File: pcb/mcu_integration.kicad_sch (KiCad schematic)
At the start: 39 parts, among them IC2 LMT87DCKT, J5 DM3BT-DSF-PEJS, U1 STM32F103RBTx, U8 LTC4300A-1IMS8_PBF, Y1 ECS-80-18-5PX-GM-TR

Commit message: Started selecting BOM
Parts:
- C1, C2, C27, C3, C4, C44, C6, C9: Manufacturer_Name (none) -> Kemet; Manufacturer_Part_Number (none) -> C0402C104K8RACAUTO
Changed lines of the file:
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@@
+			)
+		)
+		(property "Manufacturer_Name" "Kemet"
+			(at 49.53 62.23 90)
+			(effects
+				(font
+					(size 1.27 1.27)
+				)
+				(hide yes)
+			)
+		)
+		(property "Manufacturer_Part_Number" "C0402C104K8RACAUTO"
+			(at 49.53 62.23 90)
+			(effects
+				(font
+					(size 1.27 1.27)
+				)
+				(hide yes)
 			)
 		)
@@
 			)
 		)
+		(property "Manufacturer_Name" "Kemet"
+			(at 118.11 24.13 0)
+			(effects
+				(font
+					(size 1.27 1.27)
+				)
+				(hide yes)
+			)
+		)
+		(property "Manufacturer_Part_Number" "C0402C104K8RACAUTO"
+			(at 118.11 24.13 0)
+			(effects
+				(font
+					(size 1.27 1.27)
+				)
+				(hide yes)
+			)
+		)
 		(pin "1"
 		)
@@
 			)
 		)
+		(property "Manufacturer_Name" "Kemet"
+			(at 27.94 27.94 0)
+			(effects
+				(font
+					(size 1.27 1.27)
+				)
+				(hide yes)
+			)
+		)
+		(property "Manufacturer_Part_Number" "C0402C104K8RACAUTO"
+			(at 27.94 27.94 0)
+			(effects
+				(font
+					(size 1.27 1.27)
+				)
+				(hide yes)
+			)
+		)
 		(pin "1"
 		)
@@
 			)
 		)
+		(property "Manufacturer_Name" "Kemet"
+			(at 76.2 27.94 0)
+			(effects
+				(font
+					(size 1.27 1.27)
+				)
+				(hide yes)
+			)
+		)
+		(property "Manufacturer_Part_Number" "C0402C104K8RACAUTO"
+			(at 76.2 27.94 0)
+			(effects
+				(font
+					(size 1.27 1.27)
+				)
+				(hide yes)
+			)
+		)
 		(pin "1"
 		)
@@
 		)
 		(property "Description" ""
+			(at 204.47 55.88 0)
+			(effects
+				(font
+					(size 1.27 1.27)
+				)
+				(hide yes)
+			)
+		)
+		(property "Manufacturer_Name" "Kemet"
+			(at 204.47 55.88 0)
+			(effects
+				(font
+					(size 1.27 1.27)
+				)
+				(hide yes)
+			)
+		)
+		(property "Manufacturer_Part_Number" "C0402C104K8RACAUTO"
 			(at 204.47 55.88 0)
 			(effects
@@
 			)
 		)
+		(property "Manufacturer_Name" "Kemet"
+			(at 63.5 27.94 0)
+			(effects
+				(font
+					(size 1.27 1.27)
+				)
+				(hide yes)
+			)
+		)
+		(property "Manufacturer_Part_Number" "C0402C104K8RACAUTO"
+			(at 63.5 27.94 0)
+			(effects
+				(font
+					(size 1.27 1.27)
+				)
+				(hide yes)
+			)
+		)
 		(pin "1"
 		)
@@
 			)
 		)
+		(property "Manufacturer_Name" "Kemet"
+			(at 39.37 27.94 0)
+			(effects
+				(font
+					(size 1.27 1.27)
+				)
+				(hide yes)
+			)
+		)
+		(property "Manufacturer_Part_Number" "C0402C104K8RACAUTO"
+			(at 39.37 27.94 0)
+			(effects
+				(font
+					(size 1.27 1.27)
+				)
+				(hide yes)
+			)
+		)
 		(pin "1"
 		)
@@
 			(at 52.07 27.94 0)
 			(effects
+				(font
+					(size 1.27 1.27)
+				)
+				(hide yes)
+			)
+		)
+		(property "Manufacturer_Name" "Kemet"
+			(at 52.07 27.94 0)
+			(effects
+				(font
+					(size 1.27 1.27)
+				)
+				(hide yes)
+			)
+		)
+		(property "Manufacturer_Part_Number" "C0402C104K8RACAUTO"
+			(at 52.07 27.94 0)
+			(effects

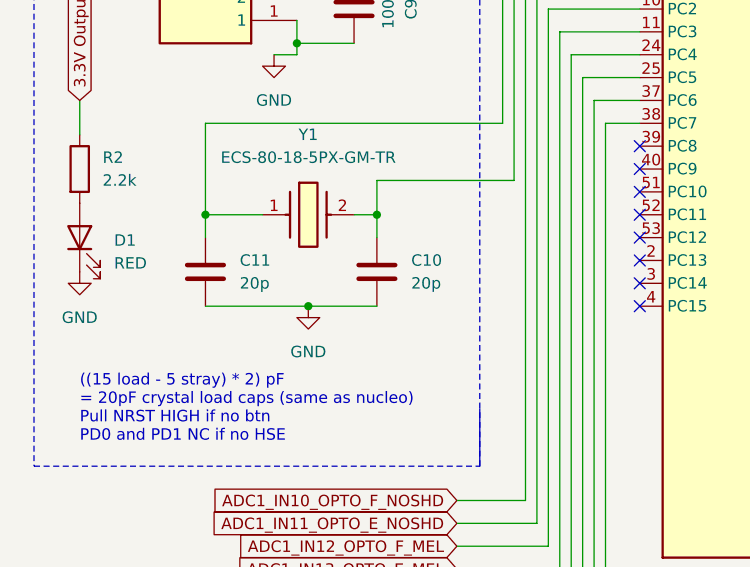
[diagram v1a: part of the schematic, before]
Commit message: Added more to the BOM
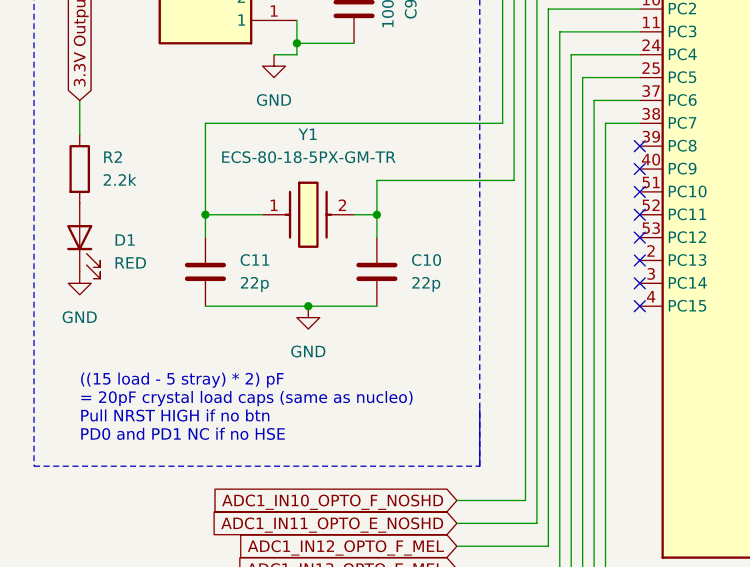
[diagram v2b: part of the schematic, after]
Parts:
- C1, C2, C27, C3, C4, C44, C6, C9: Manufacturer_Name Kemet -> Murata; Manufacturer_Part_Number C0402C104K8RACAUTO -> GCM155R71C104KA55D
- C10, C11: value 20p -> 22p; Manufacturer_Name (none) -> Murata; Manufacturer_Part_Number (none) -> GCM1555C1H220JA16D
- C33, C7, C8: Manufacturer_Name (none) -> Murata; Manufacturer_Part_Number (none) -> GRT155R61C105KE01D
- C45, C49: Manufacturer_Name (none) -> Murata; Manufacturer_Part_Number (none) -> GCM155R71H103KA55D
- C48: Manufacturer_Name (none) -> Murata; Manufacturer_Part_Number (none) -> GCM1555C1H221JA16D
- C5: Manufacturer_Name (none) -> Murata; Manufacturer_Part_Number (none) -> GRT188R61C106KE13D
- R1, R2: Manufacturer_Name (none) -> Panasonic; Manufacturer_Part_Number (none) -> ERJ-2RKF2200X
- R10, R13, R14, R9: Manufacturer_Name (none) -> Panasonic; Manufacturer_Part_Number (none) -> ERJ-H2RF1002X

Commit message: Finished BOM and fixed file paths for 3D models
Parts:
- D1, J_SWD+UART1, MH1, MH2, MH3, MH4, SH1, SH2, SH3: now not fitted
- FB1: Manufacturer_Name (none) -> Murata; Manufacturer_Part_Number (none) -> BLM18SG121TN1D
- J5: Manufacturer_Name (none) -> Hirose; Manufacturer_Part_Number (none) -> DM3BT-DSF-PEJS
- U1: Manufacturer_Name (none) -> STMicroelectronics; Manufacturer_Part_Number (none) -> STM32F103RBT7
- U8: Manufacturer_Name (none) -> Analog Devices; Manufacturer_Part_Number (none) -> LTC4300A-1IMS8#PBF
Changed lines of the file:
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@@
 		(in_bom yes)
 		(on_board yes)
-		(dnp no)
+		(dnp yes)
 		(property "Reference" "MH4"
 			(at 211.074 100.33 90)
@@
 			)
 		)
+		(property "Manufacturer_Name" "Hirose"
+			(at 219.71 33.02 0)
+			(effects
+				(font
+					(size 1.27 1.27)
+				)
+				(hide yes)
+			)
+		)
+		(property "Manufacturer_Part_Number" "DM3BT-DSF-PEJS"
+			(at 219.71 33.02 0)
+			(effects
+				(font
+					(size 1.27 1.27)
+				)
+				(hide yes)
+			)
+		)
 		(pin "5"
 		)
@@
 		(in_bom yes)
 		(on_board yes)
-		(dnp no)
+		(dnp yes)
 		(property "Reference" "SH3"
 			(at 273.05 81.534 0)
@@
 			)
 		)
+		(property "Manufacturer_Name" "STMicroelectronics"
+			(at 99.06 80.01 0)
+			(effects
+				(font
+					(size 1.27 1.27)
+				)
+				(hide yes)
+			)
+		)
+		(property "Manufacturer_Part_Number" "STM32F103RBT7"
+			(at 99.06 80.01 0)
+			(effects
+				(font
+					(size 1.27 1.27)
+				)
+				(hide yes)
+			)
+		)
 		(pin "1"
 		)
@@
 		(in_bom yes)
 		(on_board yes)
-		(dnp no)
+		(dnp yes)
 		(fields_autoplaced yes)
 		(property "Reference" "MH2"
@@
 		(in_bom yes)
 		(on_board yes)
-		(dnp no)
+		(dnp yes)
 		(fields_autoplaced yes)
 		(property "Reference" "MH3"
@@
 		(in_bom yes)
 		(on_board yes)
-		(dnp no)
+		(dnp yes)
 		(property "Reference" "SH2"
 			(at 260.35 81.534 0)
@@
 		(in_bom yes)
 		(on_board yes)
-		(dnp no)
+		(dnp yes)
 		(fields_autoplaced yes)
 		(property "Reference" "D1"
@@
 			)
 		)
+		(property "Manufacturer_Name" "Murata"
+			(at 144.78 20.32 90)
+			(effects
+				(font
+					(size 1.27 1.27)
+				)
+				(hide yes)
+			)
+		)
+		(property "Manufacturer_Part_Number" "BLM18SG121TN1D"
+			(at 144.78 20.32 90)
+			(effects
+				(font
+					(size 1.27 1.27)
+				)
+				(hide yes)
+			)
+		)
 		(pin "1"
 		)
@@
 		(in_bom yes)
 		(on_board yes)
-		(dnp no)
+		(dnp yes)
 		(property "Reference" "SH1"
 			(at 247.65 81.28 0)
@@
 		(in_bom yes)
 		(on_board yes)
-		(dnp no)
+		(dnp yes)
 		(property "Reference" "J_SWD+UART1"
 			(at 171.45 66.0399 0)
@@
 		(in_bom yes)
 		(on_board yes)
-		(dnp no)
+		(dnp yes)
 		(fields_autoplaced yes)
 		(property "Reference" "MH1"
@@
 				(hide yes)
 			)
+		)
+		(property "Manufacturer_Name" "Analog Devices"
+			(at 45.72 168.91 0)
+			(effects
+				(font
+					(size 1.27 1.27)
+				)
+				(hide yes)
+			)
+		)
+		(property "Manufacturer_Part_Number" "LTC4300A-1IMS8#PBF"
+			(at 45.72 168.91 0)
+			(effects
+				(font
+					(size 1.27 1.27)
+				)
+				(hide yes)
+			)

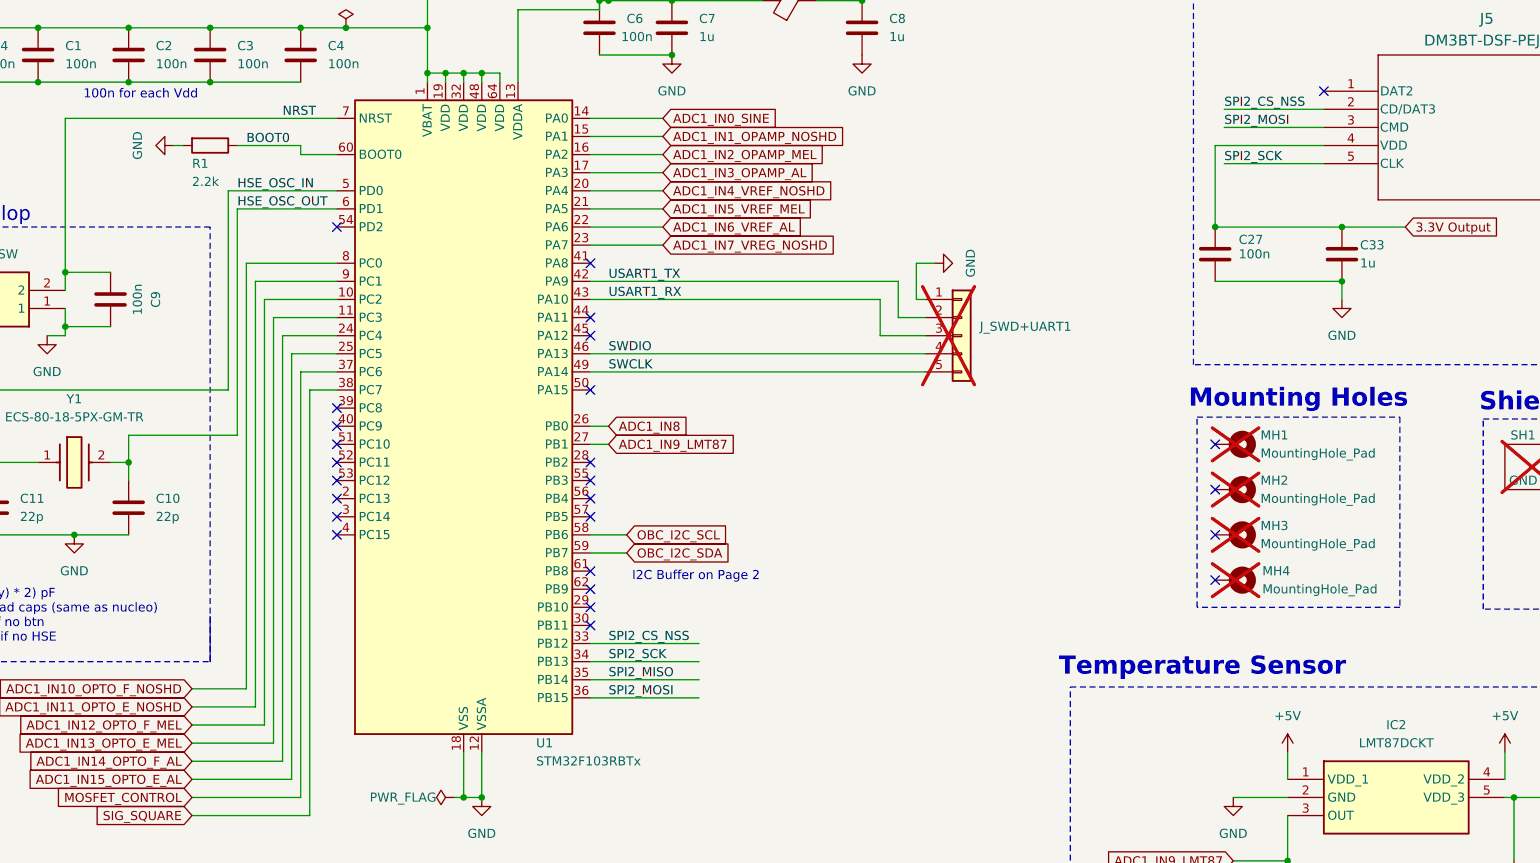
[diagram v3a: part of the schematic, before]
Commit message: updated component labels
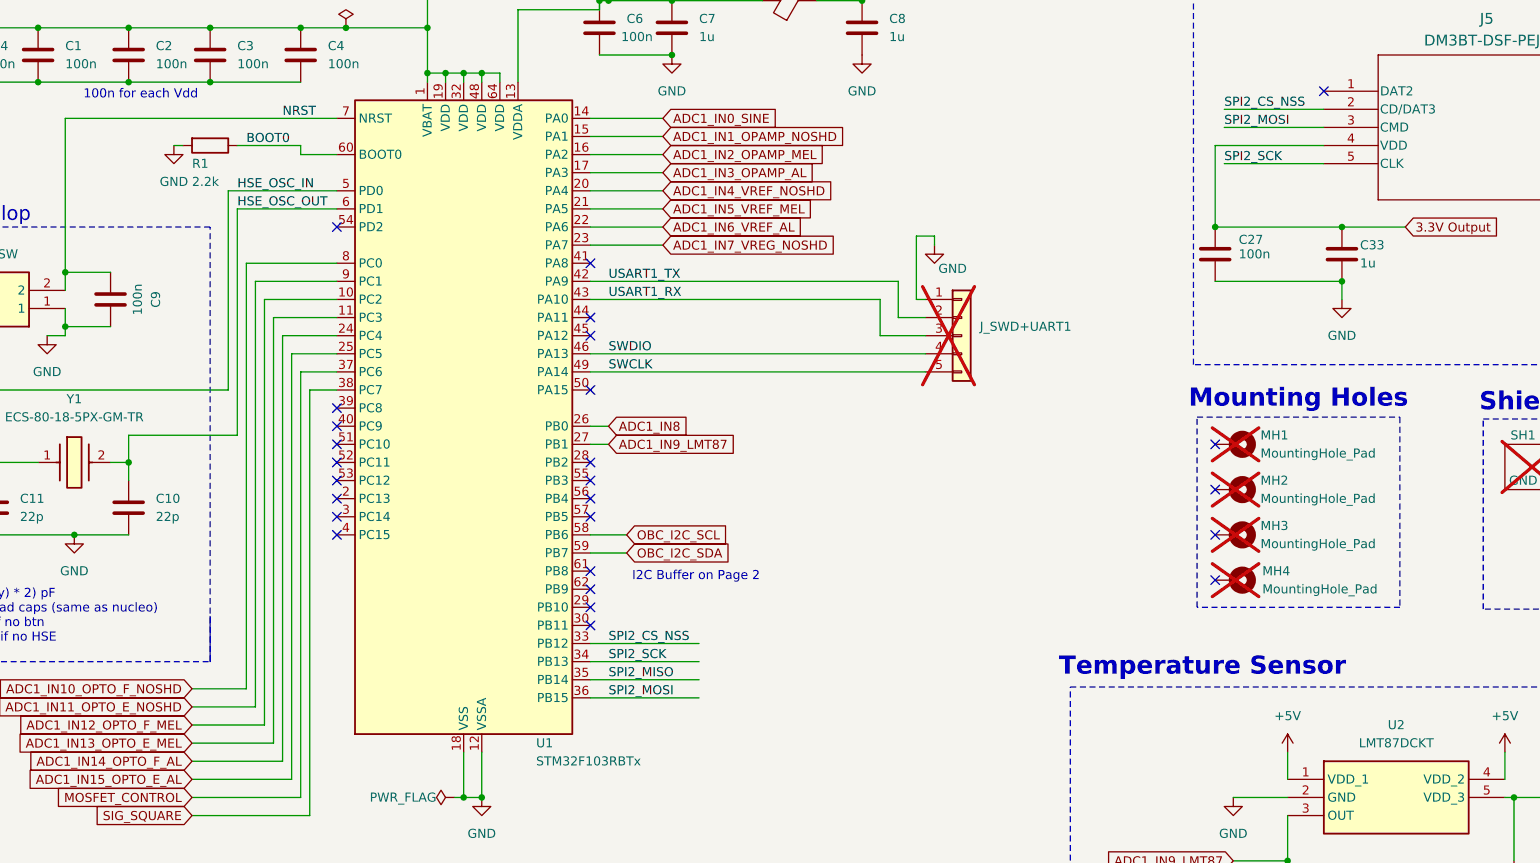
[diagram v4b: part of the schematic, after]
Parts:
- renumbered IC2 to U2
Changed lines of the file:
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@@
 	(wire
 		(pts
-			(xy 165.1 57.15) (xy 162.56 57.15)
+			(xy 165.1 53.34) (xy 162.56 53.34)
 		)
 		(stroke
@@
 	(wire
 		(pts
-			(xy 162.56 57.15) (xy 162.56 62.23)
+			(xy 162.56 53.34) (xy 162.56 62.23)
 		)
 		(stroke
@@
 	(wire
 		(pts
+			(xy 165.1 53.34) (xy 165.1 54.61)
+		)
+		(stroke
+			(width 0)
+			(type default)
+		)
+	)
+	(wire
+		(pts
 			(xy 119.38 19.05) (xy 119.38 20.32)
 		)
@@
 		(dnp no)
 		(fields_autoplaced yes)
-		(property "Reference" "IC2"
+		(property "Reference" "U2"
 			(at 229.87 121.92 0)
 			(effects
@@
 			(project ""
 				(path "/c0210bc3-f67f-47d8-a34e-f002a728adb2"
-					(reference "IC2")
+					(reference "U2")
 					(unit 1)
 				)
@@
 	(symbol
 		(lib_id "power:GND")
-		(at 165.1 57.15 90)
+		(at 165.1 54.61 0)
 		(unit 1)
 		(exclude_from_sim no)
@@
 		(on_board yes)
 		(dnp no)
-		(fields_autoplaced yes)
 		(property "Reference" "#PWR013"
-			(at 171.45 57.15 0)
+			(at 165.1 60.96 0)
 			(effects
 				(font
@@
 		)
 		(property "Value" "GND"
-			(at 170.18 57.15 0)
+			(at 167.64 57.912 0)
 			(effects
 				(font
@@
 		)
 		(property "Footprint" ""
-			(at 165.1 57.15 0)
+			(at 165.1 54.61 0)
 			(effects
 				(font
@@
 		)
 		(property "Datasheet" ""
-			(at 165.1 57.15 0)
+			(at 165.1 54.61 0)
 			(effects
 				(font
@@
 		)
 		(property "Description" ""
-			(at 165.1 57.15 0)
+			(at 165.1 54.61 0)
 			(effects
 				(font
@@
 	(symbol
 		(lib_id "power:GND")
-		(at 58.42 40.64 270)
+		(at 58.42 40.64 0)
 		(unit 1)
 		(exclude_from_sim no)
@@
 		(dnp no)
 		(property "Reference" "#PWR010"
-			(at 52.07 40.64 0)
+			(at 58.42 46.99 0)
 			(effects
 				(font
@@
 		)
 		(property "Value" "GND"
-			(at 53.34 40.64 0)
+			(at 58.42 45.72 0)
 			(effects
 				(font
